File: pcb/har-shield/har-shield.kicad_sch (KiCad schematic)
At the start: 10 parts, among them J1 Conn_01x22, J103 Conn_01x08, J104 Conn_01x05, J2 Conn_01x22

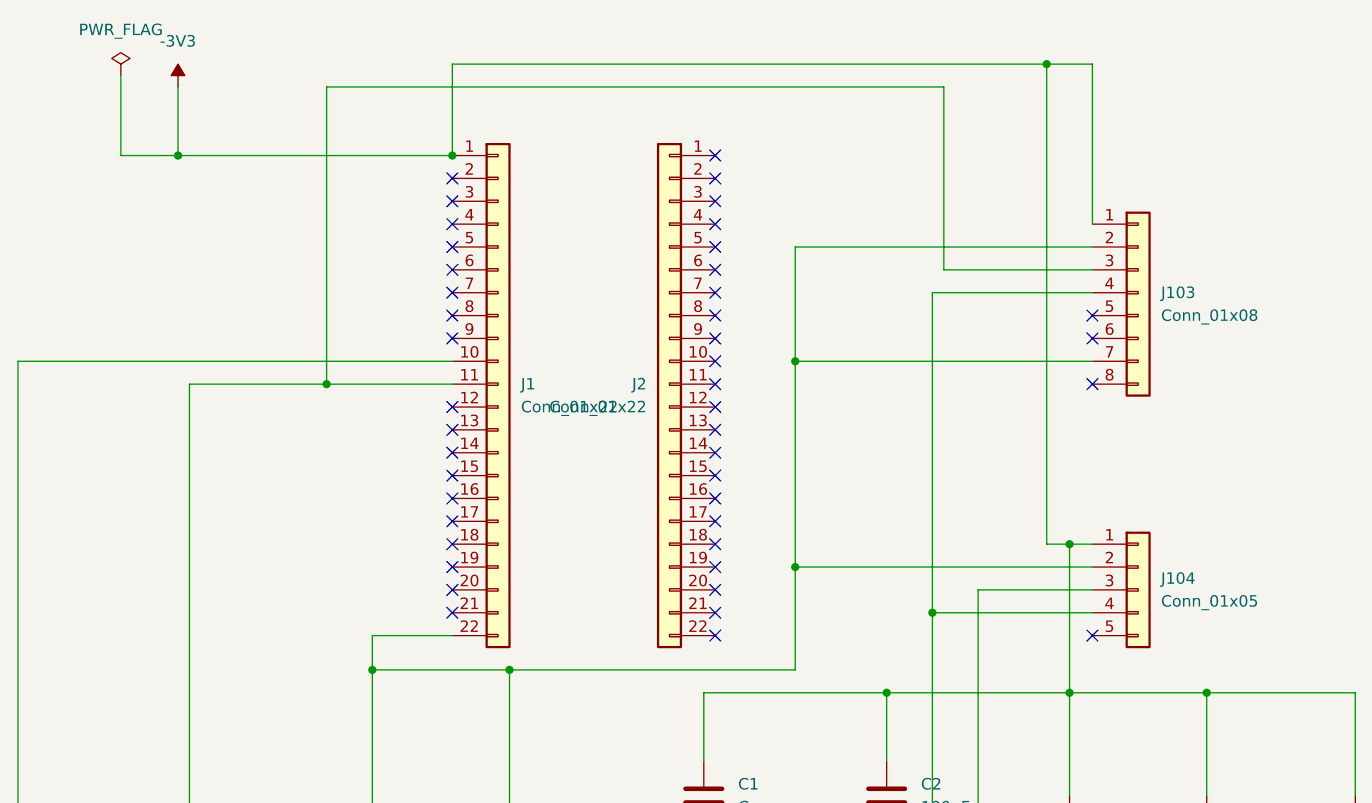
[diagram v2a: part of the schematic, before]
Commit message: D1-D10: 全链路 HAR 项目完成
## 完成内容
- D1: 项目计划书 + 采集协议 + Git骨架 + KiCad原理图
- D2: 传感器标定 (加速度计六位置 RMSE 11.35→0.42, 磁力计椭球拟合 std 1.22uT)
- D3: 9ch固件 + 预处理Pipeline + 566窗口数据集 (S01+S02 真实数据)
- D4: 294维特征提取 + 特征字典
- D5: 6种特征选择方法 + PCA/LDA/t-SNE (RFE 30维 CV 91.7%)
- D6: 6基线分类器 + MinimumRiskBayes (跌倒漏检×10)
- D7: 7高级模型 + GridSearchCV + 学习曲线
- D8: LOSO + 混淆矩阵 + McNemar (p<0.0001) + Bootstrap 95%CI
- D9: 时序平滑(MV L=7 acc 59.5%) + 1D-CNN(sit 50%) + KMeans/GMM(ARI 0.364)
- D10: 最终报告(5000字) + 答辩PPT(17页) + Demo脚本 + 一键复现 + 交付文件夹

## 硬件
- Shield PCB 焊接 + I2C验证(0x68/0x1E)
- 离线固件: 连续自动序列 + NeoPixel LED + I2C错误恢复
- 真实数据: S01+S02, 14 CSV, 566窗口

## 最佳模型
kNN (k=3,distance) + MajorityVote L=7: Accuracy 59.5%, walk 100%

Co-authored-by: 孔子瑜 <kkawo>
Co-authored-by: 李宝平 <libaoping>
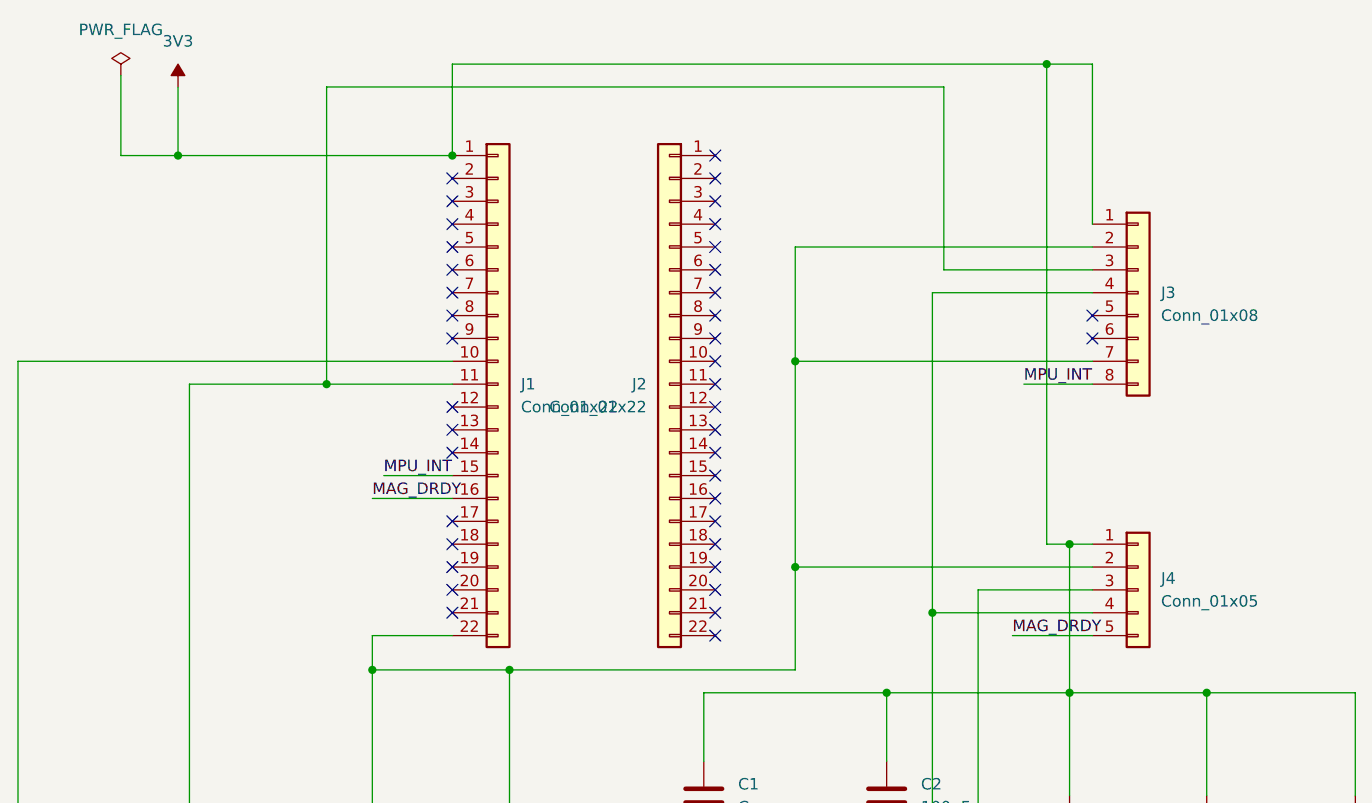
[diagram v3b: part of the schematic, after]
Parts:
- J1, J2: footprint Connector_PinHeader_2.54mm:PinHeader_1x22_P2.54mm_Vertical -> Connector_PinSocket_2.54mm:PinSocket_1x22_P2.54mm_Vertical
- J3: renamed from J103; footprint Connector_PinHeader_2.54mm:PinHeader_1x08_P2.54mm_Vertical -> Connector_PinSocket_2.54mm:PinSocket_1x08_P2.54mm_Vertical
- J4: renamed from J104; footprint Connector_PinHeader_2.54mm:PinHeader_1x05_P2.54mm_Vertical -> Connector_PinSocket_2.54mm:PinSocket_1x05_P2.54mm_Vertical
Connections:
- net MAG_DRDY: now reaches J4.5 (Pin_5)
- net MAG_DRDY: now also J1.16 (Pin_16)
- net MPU_INT: now reaches J3.8 (Pin_8)
- net MPU_INT: now also J1.15 (Pin_15)
- net -3V3 renamed 3V3
- no-connect marks 44 -> 40
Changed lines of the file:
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@@
-	)
-	(no_connect
-		(at 156.21 59.69)
 	)
 	(no_connect
@@
 	)
 	(no_connect
-		(at 85.09 72.39)
-	)
-	(no_connect
 		(at 85.09 80.01)
 	)
@@
 	)
 	(no_connect
-		(at 85.09 69.85)
-	)
-	(no_connect
-		(at 156.21 87.63)
-	)
-	(no_connect
 		(at 114.3 80.01)
 	)
@@
 	(wire
 		(pts
+			(xy 148.59 59.69) (xy 156.21 59.69)
+		)
+		(stroke
+			(width 0)
+			(type default)
+		)
+	)
+	(wire
+		(pts
 			(xy 113.03 109.22) (xy 133.35 109.22)
 		)
@@
 	(wire
 		(pts
+			(xy 77.47 69.85) (xy 85.09 69.85)
+		)
+		(stroke
+			(width 0)
+			(type default)
+		)
+	)
+	(wire
+		(pts
 			(xy 151.13 24.13) (xy 151.13 77.47)
 		)
@@
 	(wire
 		(pts
+			(xy 76.2 72.39) (xy 85.09 72.39)
+		)
+		(stroke
+			(width 0)
+			(type default)
+		)
+	)
+	(wire
+		(pts
 			(xy 151.13 24.13) (xy 85.09 24.13)
 		)
@@
 	(wire
 		(pts
+			(xy 147.32 87.63) (xy 156.21 87.63)
+		)
+		(stroke
+			(width 0)
+			(type default)
+		)
+	)
+	(wire
+		(pts
 			(xy 123.19 80.01) (xy 156.21 80.01)
 		)
@@
 			(width 0)
 			(type default)
+		)
+	)
+	(label "MAG_DRDY"
+		(at 147.32 87.63 0)
+		(effects
+			(font
+				(size 1.27 1.27)
+			)
+			(justify left bottom)
+		)
+	)
+	(label "MPU_INT"
+		(at 148.59 59.69 0)
+		(effects
+			(font
+				(size 1.27 1.27)
+			)
+			(justify left bottom)
+		)
+	)
+	(label "MPU_INT"
+		(at 77.47 69.85 0)
+		(effects
+			(font
+				(size 1.27 1.27)
+			)
+			(justify left bottom)
+		)
+	)
+	(label "MAG_DRDY"
+		(at 76.2 72.39 0)
+		(effects
+			(font
+				(size 1.27 1.27)
+			)
+			(justify left bottom)
 		)
 	)
@@
 		(dnp no)
 		(fields_autoplaced yes)
-		(property "Reference" "J104"
+		(property "Reference" "J4"
 			(at 163.83 81.2799 0)
 			(show_name no)
@@
 			)
 		)
-		(property "Footprint" "Connector_PinHeader_2.54mm:PinHeader_1x05_P2.54mm_Vertical"
+		(property "Footprint" "Connector_PinSocket_2.54mm:PinSocket_1x05_P2.54mm_Vertical"
 			(at 161.29 82.55 0)
 			(hide yes)
@@
 			(project "har-shield"
 				(path "/3ab08d95-1261-4d51-b5b6-6f7bc70db9bb"
-					(reference "J104")
+					(reference "J4")
 					(unit 1)
 				)
@@
 		(dnp no)
 		(fields_autoplaced yes)
-		(property "Reference" "J103"
+		(property "Reference" "J3"
 			(at 163.83 49.5299 0)
 			(show_name no)
@@
 			)
 		)
-		(property "Footprint" "Connector_PinHeader_2.54mm:PinHeader_1x08_P2.54mm_Vertical"
+		(property "Footprint" "Connector_PinSocket_2.54mm:PinSocket_1x08_P2.54mm_Vertical"
 			(at 161.29 49.53 0)
 			(hide yes)
@@
 			(project "har-shield"
 				(path "/3ab08d95-1261-4d51-b5b6-6f7bc70db9bb"
-					(reference "J103")
+					(reference "J3")
 					(unit 1)
 				)
@@
 			)
 		)
-		(property "Footprint" "Connector_PinHeader_2.54mm:PinHeader_1x22_P2.54mm_Vertical"
+		(property "Footprint" "Connector_PinSocket_2.54mm:PinSocket_1x22_P2.54mm_Vertical"
 			(at 109.22 59.69 0)
 			(hide yes)
@@
 			)
 		)
-		(property "Footprint" "Connector_PinHeader_2.54mm:PinHeader_1x22_P2.54mm_Vertical"
+		(property "Footprint" "Connector_PinSocket_2.54mm:PinSocket_1x22_P2.54mm_Vertical"
 			(at 90.17 59.69 0)
 			(hide yes)
@@
 			)
 		)
-		(property "Value" "-3V3"
+		(property "Value" "3V3"
 			(at 54.61 21.59 0)
 			(show_name no)
